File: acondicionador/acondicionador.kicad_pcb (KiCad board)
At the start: 2 copper layers, 89.4 x 79.2 mm, 35 parts, among them J1 VC_24V, J2 Ant, J4 SMA, U1 TL084, U2 TL082, U3 LM7818_TO220, U4 AD620

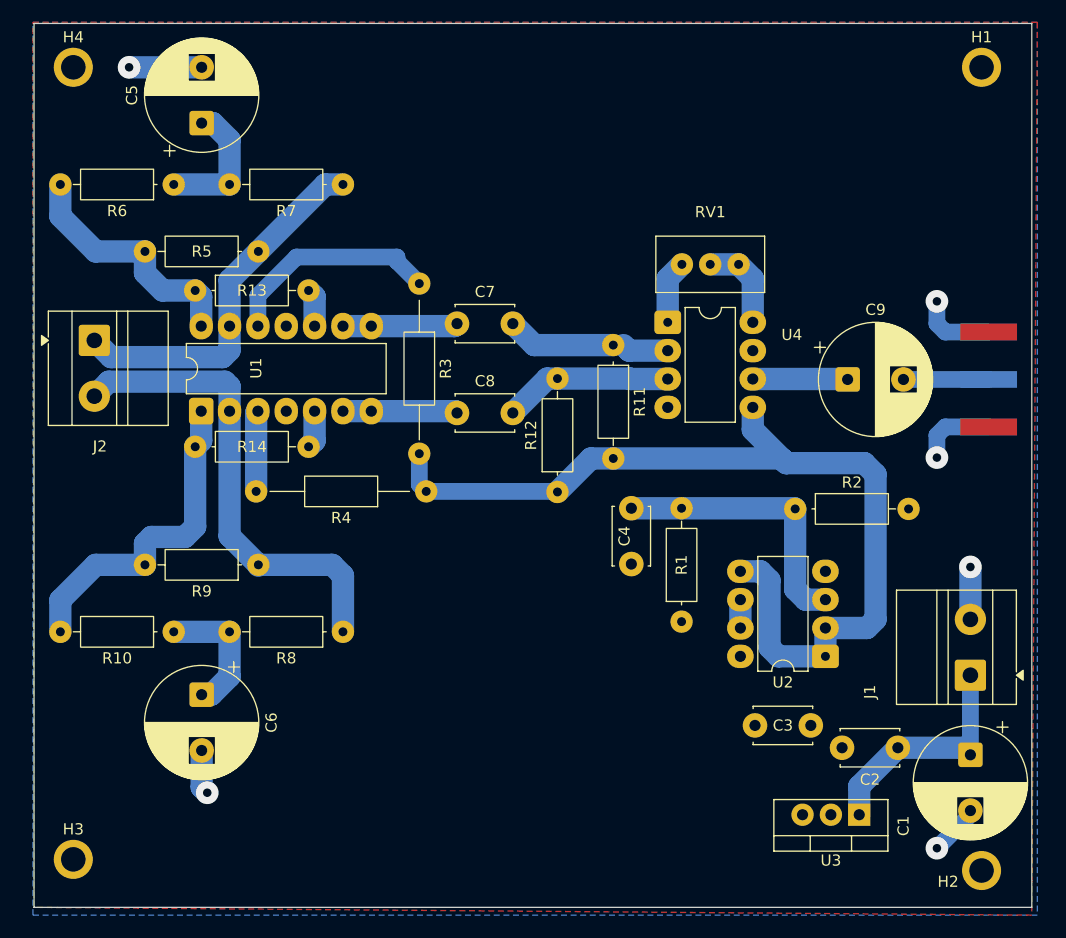
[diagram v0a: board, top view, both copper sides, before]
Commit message: Modificación posición C5 C6 en placa Acondicionador y cambio de huella sma (verificar), cambio de huella sma en placa Adquisición (verificar)
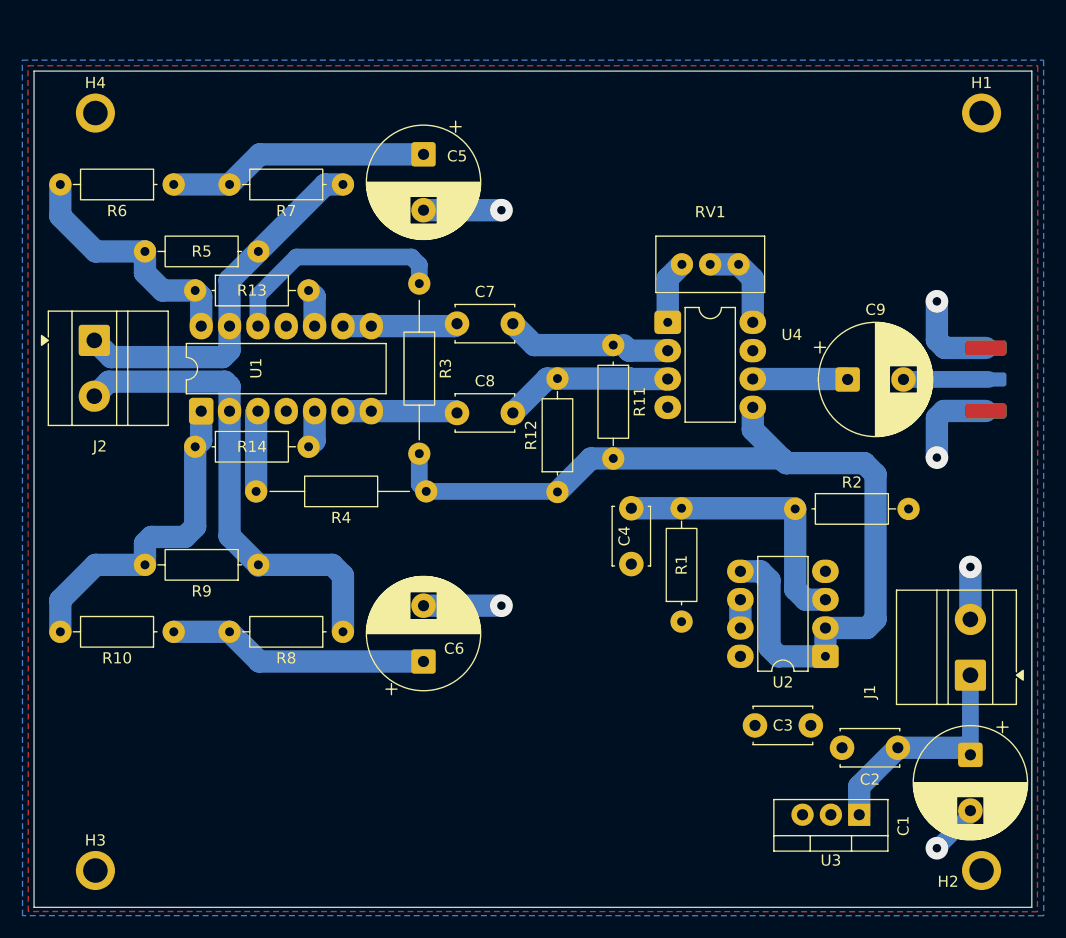
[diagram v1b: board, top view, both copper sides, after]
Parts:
- J4: footprint Connector_Coaxial:SMA_Amphenol_132289_EdgeMount -> Connector_Coaxial:SMA_Samtec_SMA-J-P-H-ST-EM1_EdgeMount
- moved C6 20.1 mm to (165.0, 107.3), turned to 90 degrees
- moved C5 20.1 mm to (165.0, 61.8), turned to -90 degrees
- moved H4 4.55 mm to (135.6, 58.1)
- moved H1 4.10 mm to (215.0, 58.1)
- moved H3 2.22 mm to (135.6, 126.0)
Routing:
- net Net-(C5-Pad1): track 12.1 -> 23.5 mm
- net Net-(C6-Pad1): track 12.2 -> 23.5 mm
- net GND: track 33.7 -> 39.6 mm
- net Net-(U1D-+): track 19.8 -> 20.6 mm
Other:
- board size 89.4 x 79.2 mm -> 89.4 x 74.9 mm

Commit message: se modifica la disposición de los elementos
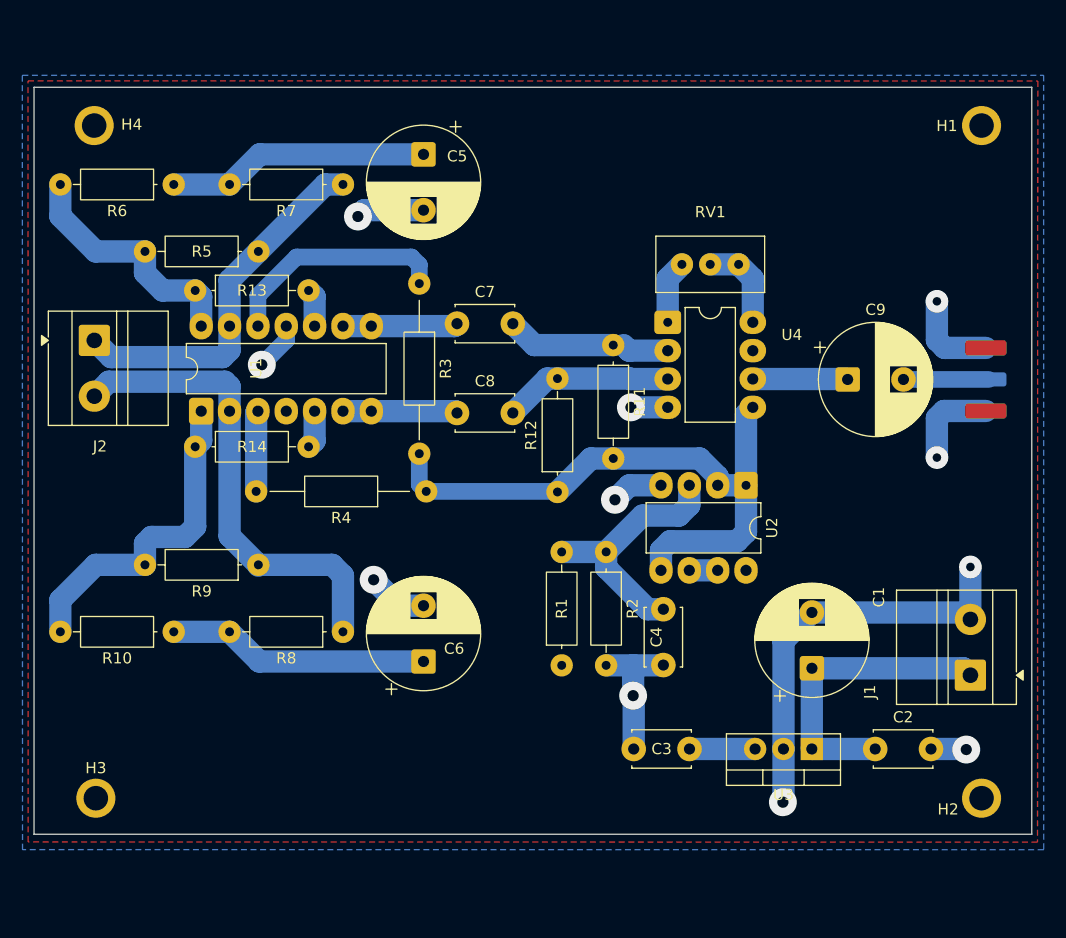
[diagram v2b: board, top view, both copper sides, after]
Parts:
- moved R2 17.4 mm to (181.4, 97.5), turned to -90 degrees
- moved U2 16.9 mm to (193.9, 91.5), turned to -90 degrees
- moved C1 16.2 mm to (199.8, 107.9), turned to 90 degrees
- moved R1 11.4 mm to (177.4, 107.6)
- moved C4 9.49 mm to (186.5, 102.6)
- moved U3 7.26 mm to (199.8, 115.1)
- moved H3 6.48 mm to (135.6, 119.5)
- moved H2 6.48 mm to (215.0, 119.5)
- moved C3 6.24 mm to (188.8, 115.1), turned to 180 degrees
- moved C2 2.03 mm to (205.5, 115.1), turned to 0 degrees
- moved H4 1.13 mm to (135.5, 59.2)
- moved H1 1.12 mm to (215.0, 59.2)
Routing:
- net GND: track 39.6 -> 93.4 mm, vias 6 -> 11
- net Vq: track 86.6 -> 56.5 mm
- net Net-(J1-Pin_1): track 21.3 -> 27.4 mm
- net VCC: track 0.00 -> 5.88 mm
- net Net-(U2A-+): track 25.0 -> 23.0 mm
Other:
- board size 89.4 x 74.9 mm -> 89.4 x 66.9 mm

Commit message: Compensación Voi acondicionador
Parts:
- added R15: 750k, huellas_proyecto:R_Axial_DIN0207_L6.3mm_D2.5mm_P10.16mm_Horizontal-pad2mm, F.Cu at (169.5, 71.3)
- added RV2: 10k, huellas_proyecto:Potentiometer_Bourns_3296W_Vertical-pad2mm, F.Cu at (182.3, 63.7)
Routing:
- net Net-(R15-Pad2): track 0.00 -> 7.63 mm
- net Net-(U1D-+): track 20.6 -> 25.7 mm
